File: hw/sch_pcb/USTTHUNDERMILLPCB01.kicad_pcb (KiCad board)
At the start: 4 copper layers, 80 x 80 mm, 70 parts, among them J1 SM04B-GHS-TB, J2 SM03B-GHS-TB, J4 HEADER_2x03, J5 SM08B-GHS-TB, J6 SM06B-GHS-TB, SW1 KMT031 NGJ LHS C&K, U1 ISL21080DIH312Z-TK 1V25, U2 OPA314, U3 MIC5504-3.3YM5, U4 PCF8583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

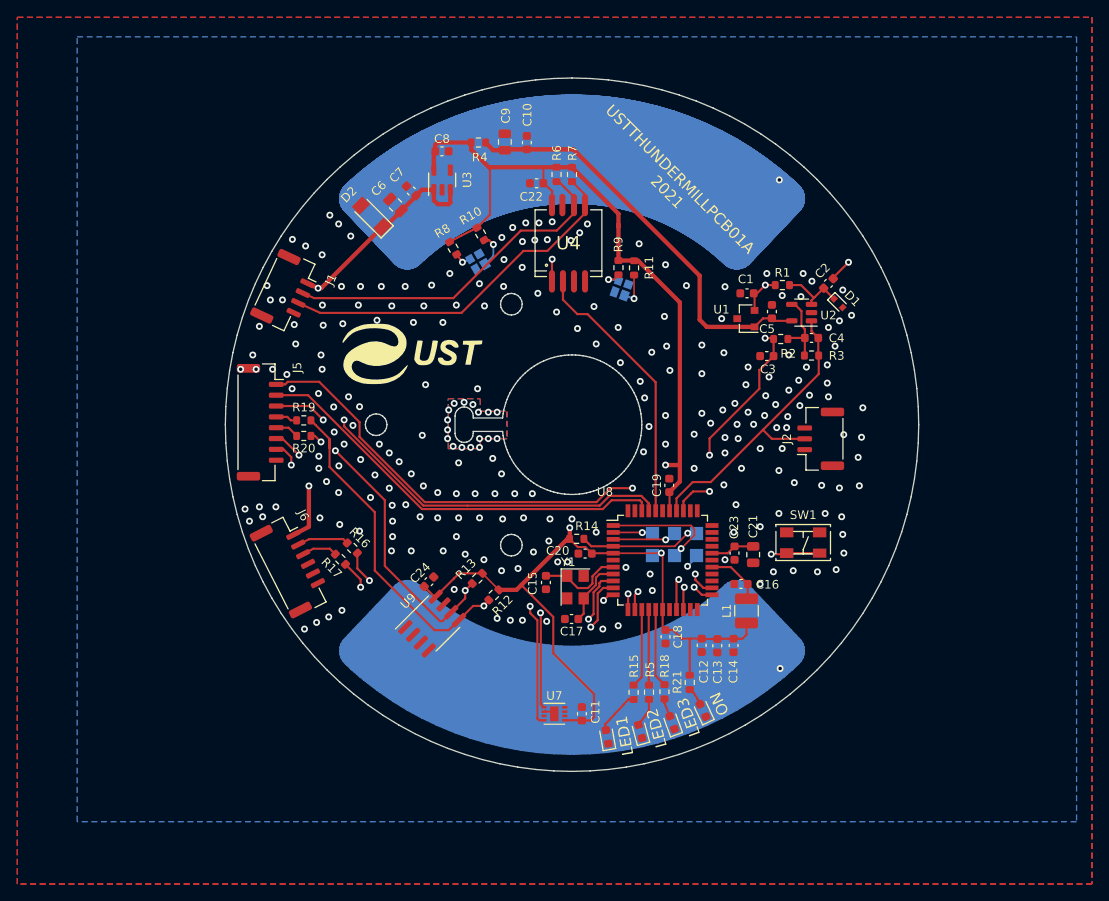
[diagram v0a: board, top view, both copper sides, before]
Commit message: updates of schematics and layout: solve: #6, #3, #8, #10
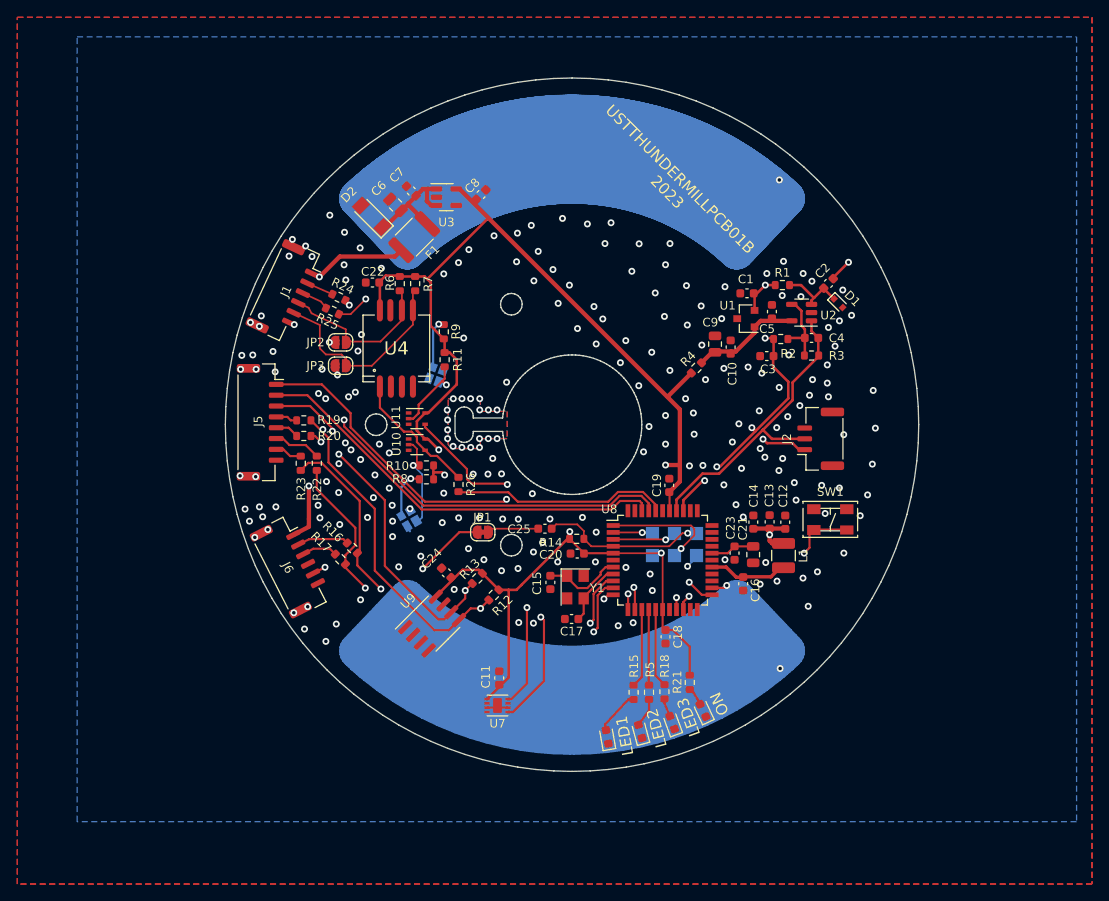
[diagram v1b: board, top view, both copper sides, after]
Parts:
- removed G*** (x2): LOGO, MLAB_LOGA:UST
- added C25: 4u7, Capacitor_SMD:C_0603_1608Metric, F.Cu at (139.4, 104.5)
- added F1: 350mA, Fuse:Fuse_1812_4532Metric, F.Cu at (124.3, 70.8)
- added JP1: SolderJumper_2_Bridged, Jumper:SolderJumper-2_P1.3mm_Bridged_RoundedPad1.0x1.5mm, F.Cu at (132.2, 104.9)
- added JP2: SolderJumper_2_Open, Jumper:SolderJumper-2_P1.3mm_Open_RoundedPad1.0x1.5mm, F.Cu at (115.8, 83.0)
- added JP3: SolderJumper_2_Open, Jumper:SolderJumper-2_P1.3mm_Open_RoundedPad1.0x1.5mm, F.Cu at (115.8, 85.7)
- added R22: 33R, Resistor_SMD:R_0603_1608Metric, F.Cu at (113.0, 97.0)
- added R23: 33R, Resistor_SMD:R_0603_1608Metric, F.Cu at (111.2, 97.0)
- added R24: 33R, Resistor_SMD:R_0603_1608Metric, F.Cu at (115.6, 77.8)
- added R25: 33R, Resistor_SMD:R_0603_1608Metric, F.Cu at (114.9, 79.4)
- added R26: 33R, Resistor_SMD:R_0603_1608Metric, F.Cu at (129.4, 99.4)
- added U10: SN74LVC1G14QDCKRQ1, Package_TO_SOT_SMD:SOT-353_SC-70-5, F.Cu at (124.6, 94.8)
- added U11: SN74LVC1G14QDCKRQ1, Package_TO_SOT_SMD:SOT-353_SC-70-5, F.Cu at (124.6, 91.8)
- J1: value SM04B-GHS-TB -> SM06B-GHS-TB; footprint Connector_JST:JST_GH_SM04B-GHS-TB_1x04-1MP_P1.25mm_Horizontal -> Connector_JST:JST_GH_SM06B-GHS-TB_1x06-1MP_P1.25mm_Horizontal
- moved R4 36.2 mm to (156.8, 86.0), turned to -135 degrees
- moved C9 33.6 mm to (159.0, 83.2)
- moved C10 33.3 mm to (160.8, 83.5)
- moved U5 30.7 mm to (123.7, 103.3)
- moved R10 27.4 mm to (125.7, 97.2), turned to 180 degrees
- moved R8 26.8 mm to (125.7, 98.8), turned to 180 degrees
- moved R11 24.3 mm to (127.8, 85.0)
- moved U6 23.6 mm to (126.8, 86.8)
- moved U4 23.3 mm to (122.2, 83.7)
- moved C22 22.1 mm to (119.5, 76.1)
- moved R6 22.0 mm to (122.6, 76.2)
- moved R7 22.0 mm to (124.4, 76.2)
- moved R9 21.5 mm to (127.7, 81.8), turned to 90 degrees
- moved C12 17.2 mm to (167.1, 103.8), turned to 90 degrees
- moved C13 15.5 mm to (165.3, 103.7), turned to 90 degrees
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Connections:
- C6 pad 1: +5V -> Net-(C6-Pad1)
- C7 pad 1: +5V -> Net-(C6-Pad1)
- D2 pad 1: +5V -> Net-(C6-Pad1)
- J1 pad 2: /tachometer/SCL -> Net-(J1-Pad2)
- J1 pad 3: /tachometer/SDA -> Net-(J1-Pad3)
- J1 pad 4: ROTOR_GND -> SCL_RPM
- J2 pad 1: ROTOR_GND -> PA1
- J5 pad 6: /CPU/TX1 -> Net-(J5-Pad6)
- J5 pad 7: /CPU/RX1 -> Net-(J5-Pad7)
- J6 pad 5: unconnected-(J6-Pad5) -> Net-(J6-Pad5)
- R10 pad 2: /tachometer/COUNT_1 -> Net-(R10-Pad2)
- R11 pad 2: COUNT_2 -> Net-(R11-Pad2)
- R6 pad 2: /tachometer/SCL -> SCL_RPM
- R7 pad 2: /tachometer/SDA -> SDA_RPM
- U3 pad 1: +5V -> Net-(C6-Pad1)
- U3 pad 3: +5V -> Net-(C6-Pad1)
- U4 pad 1: /tachometer/COUNT_1 -> COUNT_1
- U4 pad 2: COUNT_1_PCFO -> unconnected-(U4-Pad2)
- U4 pad 5: /tachometer/SDA -> SDA_RPM
- U4 pad 6: /tachometer/SCL -> SCL_RPM
- U5 pad 2: /tachometer/COUNT_1 -> Net-(R10-Pad2)
- U6 pad 2: COUNT_2 -> Net-(R11-Pad2)
- U8 pad 40: COUNT_1_PCFO -> Net-(R26-Pad2)
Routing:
- net (no net): track 503.9 -> 126.0 mm
- net /CPU/BTN: track 18.3 -> 145.6 mm
- net /tachometer/SDA: track 42.4 -> 0.00 mm
- net /tachometer/SCL: track 40.1 -> 0.00 mm
- net +3.3VP: track 47.7 -> 12.8 mm
- net COUNT_1_PCFO: track 31.6 -> 0.00 mm
- net Net-(R26-Pad2): track 0.00 -> 24.7 mm
- net SDA_RPM: track 0.00 -> 24.0 mm
- net Net-(J6-Pad5): track 0.00 -> 21.4 mm, vias 0 -> 2
- net SCL_RPM: track 0.00 -> 18.7 mm
- net COUNT_1: track 0.00 -> 15.2 mm
- net /CPU/RX0: track 38.3 -> 53.3 mm
- net Net-(C6-Pad1): track 0.00 -> 14.1 mm
- net /tachometer/COUNT_1: track 14.0 -> 0.00 mm, vias 2 -> 0
- net /CPU/TX0: track 38.8 -> 52.5 mm
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- removed copper zone on B.Cu, net PA1
- removed copper zone on F.Cu, net PA1
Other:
- board text added: "Debug UART"
- board text added: "Payload"
- board text added: "Pixhawk I2C & UART"
- board text added: "USTTHUNDERMILLPCB01B 2023"
- board text removed: "USTTHUNDERMILLPCB01A 2021"

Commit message: uprava silkscreenu, pridani popisku konektoru
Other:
- board text added: "Connectors: J1 - Pixhawk UART & I2C J5 - Payload connector J6 - Debug & programming J2 - Measuring signal"
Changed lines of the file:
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@@
     (property "UST_ID" "5fa0f70212875025b3977932")
     (attr smd)
-    (fp_text reference "J1" (at 0 0 -115) (layer "F.SilkS")
+    (fp_text reference "J1" (at 4.930461 -2.795632 -115) (layer "F.SilkS")
       (effects (font (size 1 1) (thickness 0.15)))
     )
@@
     (property "UST_ID" "5fa0f70212875025b3977932")
     (attr smd)
-    (fp_text reference "J6" (at -0.04223 0.437514 117) (layer "F.SilkS")
+    (fp_text reference "J6" (at 5.03609 -2.811049 117) (layer "F.SilkS")
       (effects (font (size 1 1) (thickness 0.15)))
     )
@@
     (property "UST_ID" "612880e51287500165a978de")
     (attr smd)
-    (fp_text reference "J2" (at 0 -3.9 90) (layer "F.SilkS")
+    (fp_text reference "J2" (at -2.9176 -2.596 90) (layer "F.SilkS")
       (effects (font (size 1 1) (thickness 0.15)))
     )
@@
     (property "UST_ID" "5fa0f75012875025b3977948")
     (attr smd)
-    (fp_text reference "J5" (at -0.123129 0.218484 90) (layer "F.SilkS")
+    (fp_text reference "J5" (at 6.176871 -2.881516 90) (layer "F.SilkS")
       (effects (font (size 1 1) (thickness 0.15)))
     )
@@
     (effects (font (size 1.3 1.3) (thickness 0.3)))
   )
+  (gr_text "Connectors:\n\nJ1 - Pixhawk UART & I2C\nJ5 - Payload connector\nJ6 - Debug & programming\nJ2 - Measuring signal" (at 146.25 61 180) (layer "F.SilkS")
+    (effects (font (size 1 1) (thickness 0.15)) (justify left))
+  )
   (gr_text "LED1" (at 148.59 128.397 100) (layer "F.SilkS")
     (effects (font (size 1.3 1.3) (thickness 0.3)))
@@
     (effects (font (size 1.3 1.3) (thickness 0.3)))
   )
-  (gr_text "USTTHUNDERMILLPCB01B\n2023" (at 154.2288 64.9224 315) (layer "F.SilkS")
+  (gr_text "USTTHUNDERMILLPCB01B\n2023" (at 160.7 62.65 135) (layer "F.SilkS")
     (effects (font (size 1.3 1.3) (thickness 0.3)))
   )

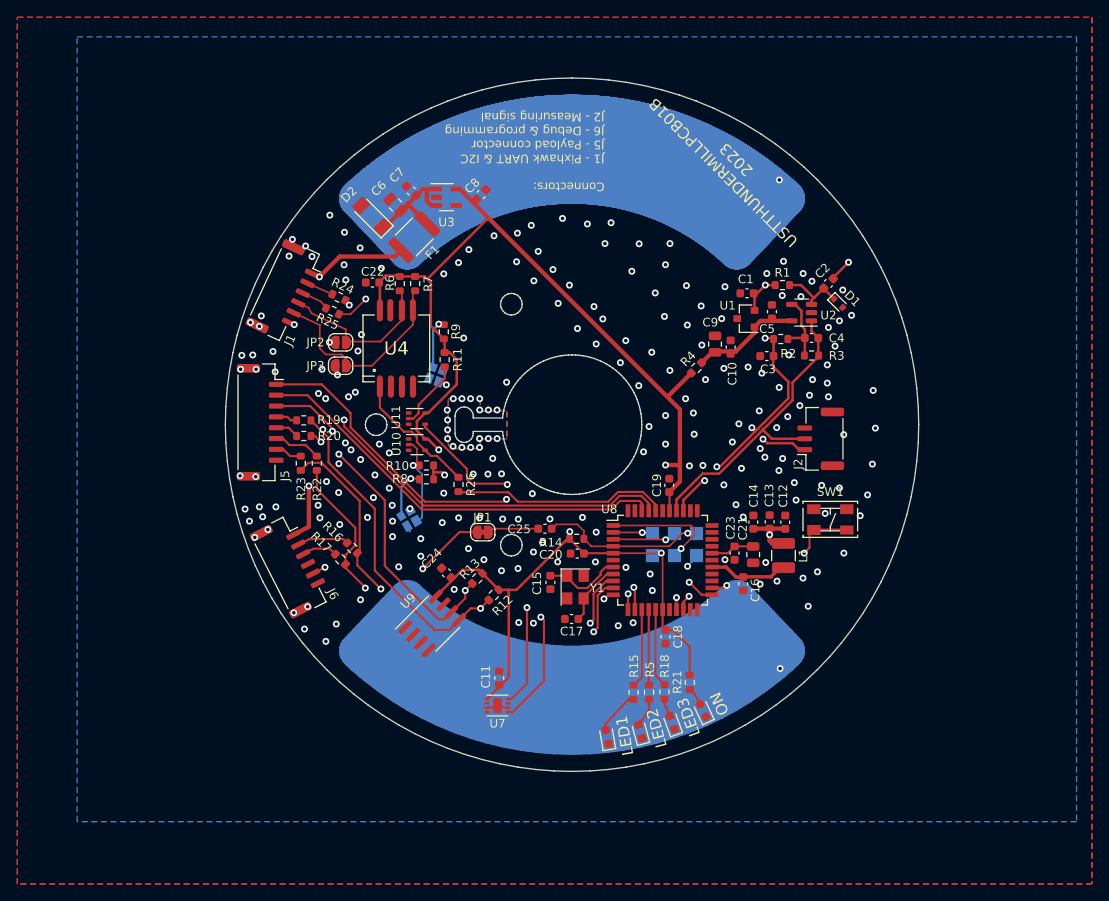
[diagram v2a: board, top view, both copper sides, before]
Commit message: Update layout, add 3rd position sensor
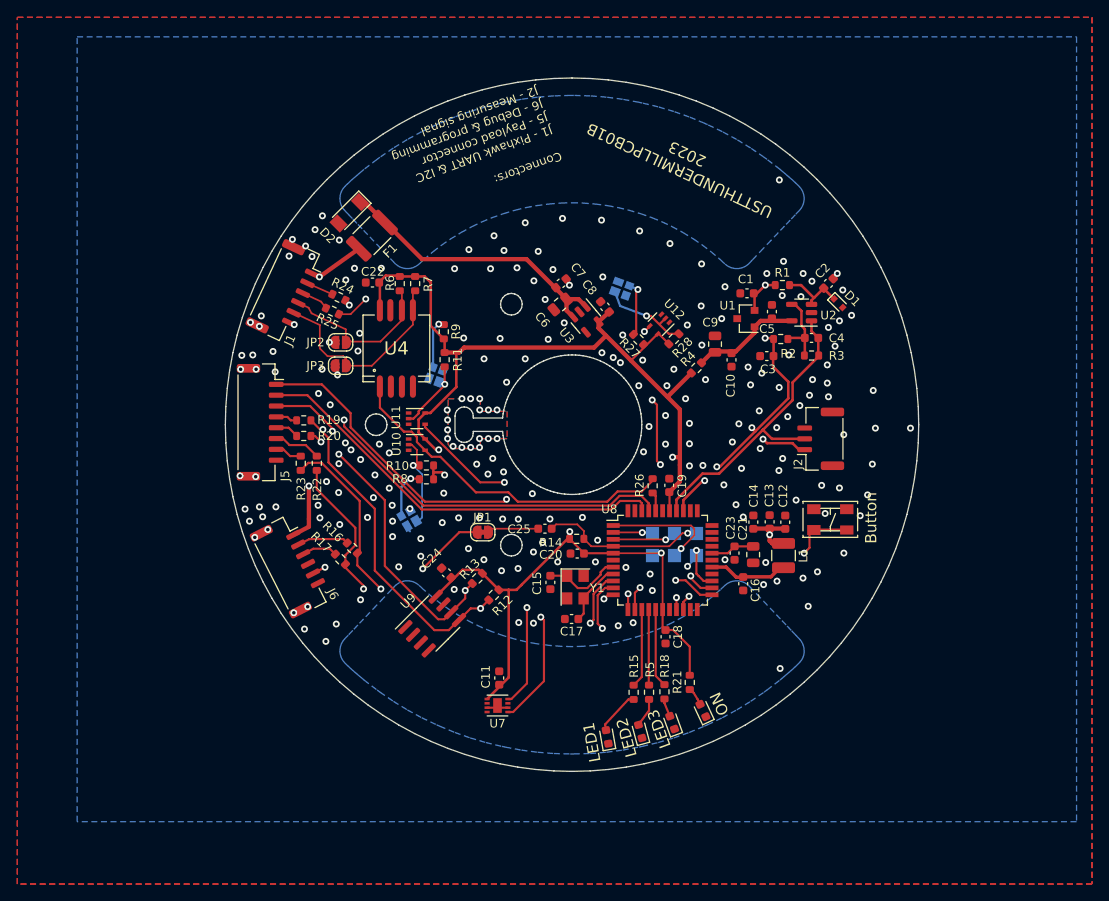
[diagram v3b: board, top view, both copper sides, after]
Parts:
- added R27: 100R, Resistor_SMD:R_0603_1608Metric, F.Cu at (150.2, 82.7)
- added R28: 4k7, Resistor_SMD:R_0603_1608Metric, F.Cu at (154.2, 82.6)
- added U12: SN74LVC1G14QDCKRQ1, Package_TO_SOT_SMD:SOT-353_SC-70-5, F.Cu at (152.6, 80.9)
- added U13: VCNT2020, Mlab_IO:XDCR_VCNT2020, B.Cu at (148.2, 76.8)
- moved R26 22.4 mm to (151.8, 99.5)
- moved C6 22.2 mm to (141.1, 78.6), turned to -140 degrees
- moved U3 21.4 mm to (144.1, 80.3), turned to -50 degrees
- moved C7 20.3 mm to (141.2, 76.2), turned to 40 degrees
- moved C8 19.3 mm to (146.3, 78.9), turned to 130 degrees
- moved F1 4.89 mm to (119.4, 70.7)
- moved D2 2.61 mm to (116.8, 68.0), turned to -135 degrees
- moved C10 1.48 mm to (160.9, 85.0), turned to -90 degrees
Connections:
- U8 pad 25: unconnected-(U8-Pad25) -> COUNT_3
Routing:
- net STATOR: track 133.5 -> 2.49 mm
- net (no net): track 126.0 -> 0.00 mm
- net /CPU/BTN: track 145.6 -> 24.2 mm
- net COUNT_3: track 0.00 -> 35.1 mm, vias 0 -> 5
- net COUNT_1: track 15.2 -> 40.0 mm
- net Net-(R26-Pad2): track 24.7 -> 2.20 mm
- net Net-(C6-Pad1): track 14.1 -> 32.9 mm
- net Net-(R28-Pad2): track 0.00 -> 10.5 mm, vias 0 -> 1
- net Net-(R27-Pad2): track 0.00 -> 6.47 mm, vias 0 -> 1
- net +3V3: track 204.0 -> 198.0 mm
- net +5V: track 42.1 -> 37.0 mm
- net /CPU/RX1: track 59.0 -> 55.6 mm
- net /CPU/TX1: track 63.9 -> 60.6 mm
- net ROTOR_GND: track 4.64 -> 2.97 mm, vias 216 -> 210
- net Net-(R11-Pad2): track 9.57 -> 8.45 mm
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- added copper zone on In1.Cu, net STATOR
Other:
- board text added: "Button"

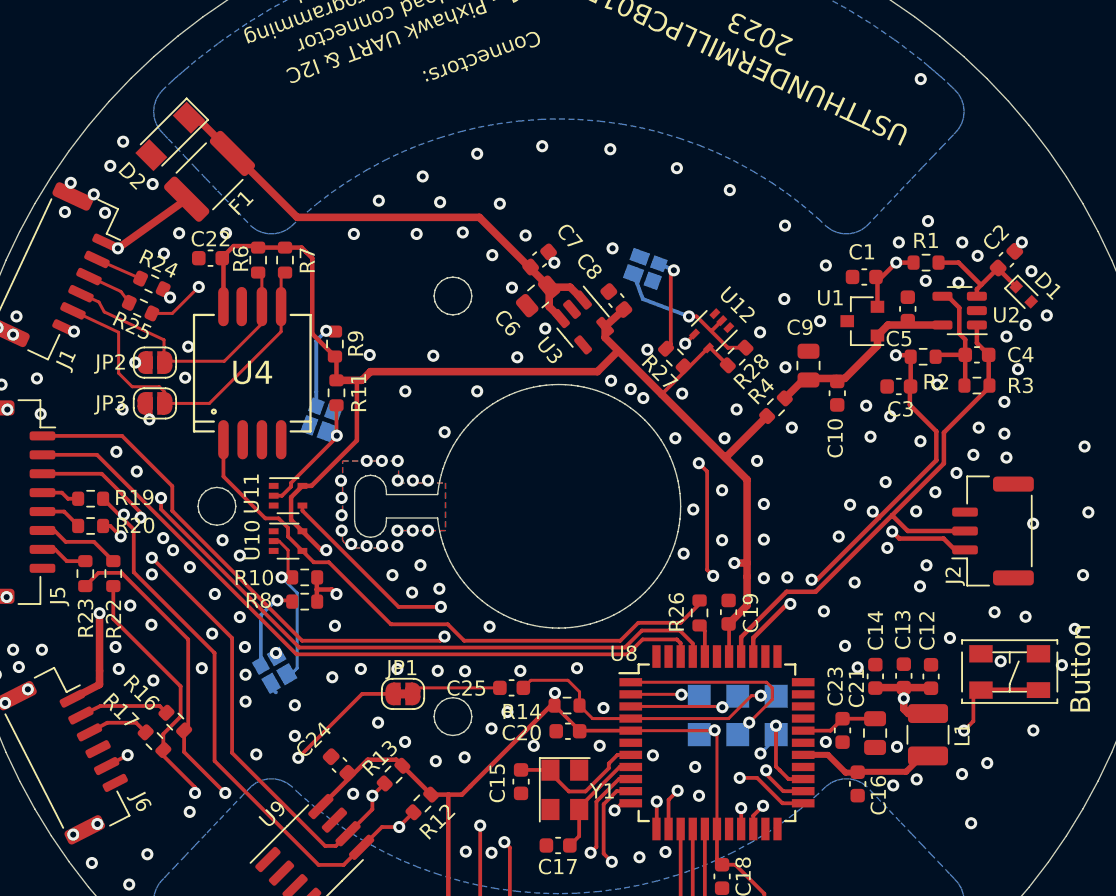
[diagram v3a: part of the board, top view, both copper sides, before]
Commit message: solve DRC, check ERC
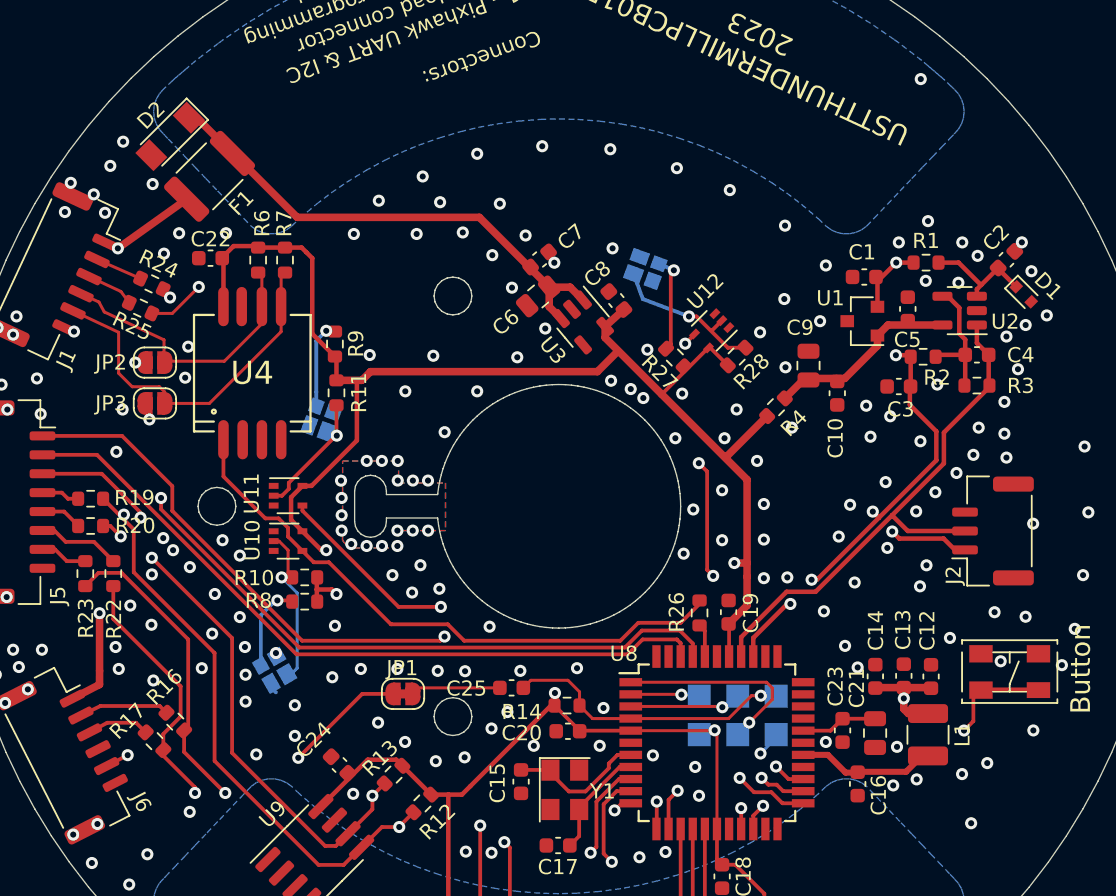
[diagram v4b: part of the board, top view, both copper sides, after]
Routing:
- net ROTOR_GND: track 2.97 -> 4.64 mm
- net COUNT_3: track 35.1 -> 33.5 mm, vias 5 -> 4
